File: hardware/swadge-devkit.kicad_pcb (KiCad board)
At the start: 2 copper layers, 63.7 x 100 mm, 61 parts, among them J1 USB_B_Micro, SW1 SW_SPDT, SW2 4-1437565-2, SW3 4-1437565-2, SW4 4-1437565-2, SW5 4-1437565-2, U1 ESP-13-WROOM-02D, U2 MCP6001-OT, U3 MSA300, U4 AP1117-33, U5 BUS_PCIexpress, U6 DISP_OLED_UG-2864HSWEG01, U7 SAO, U9 MMA8452Q

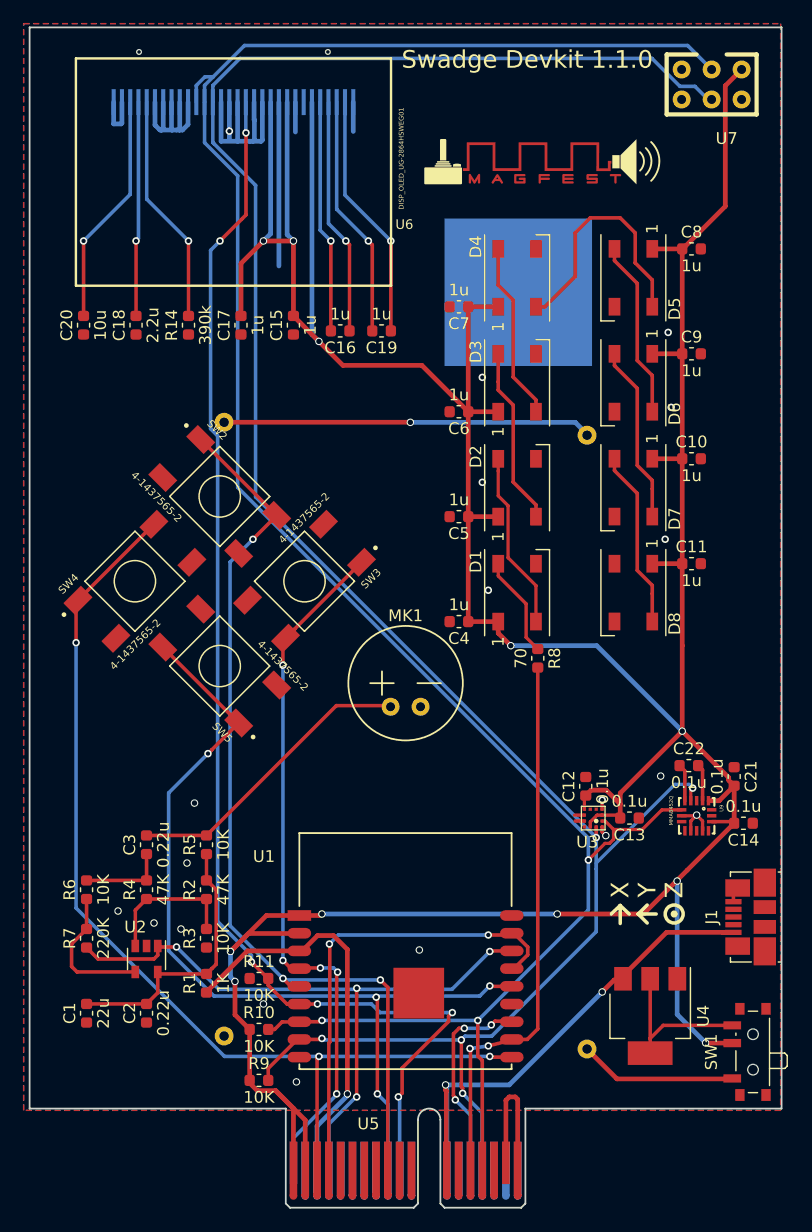
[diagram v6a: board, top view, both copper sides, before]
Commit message: #17 Reordered PCIe connector for WROOM sanity
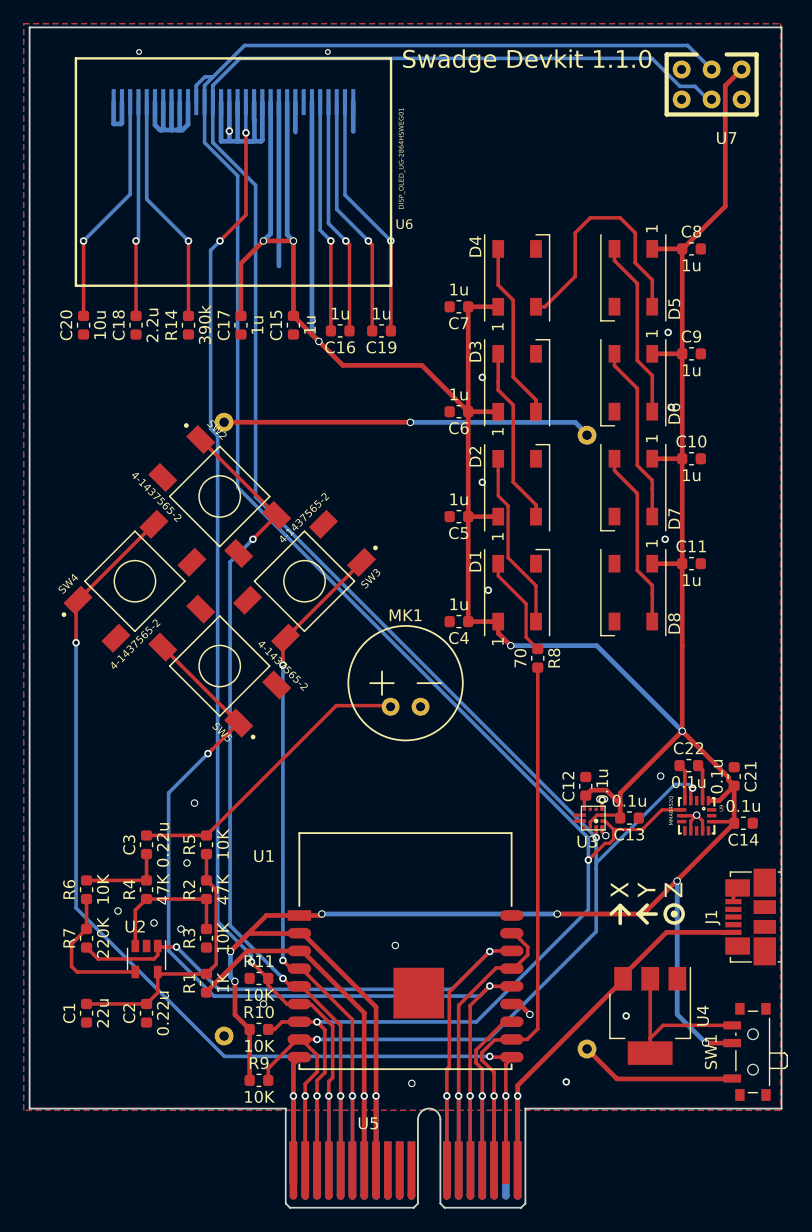
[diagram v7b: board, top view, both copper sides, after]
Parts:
- removed svg2mod: G***, Swadge_Parts:pcb_color_swatches
- removed svg2mod: G***, Swadge_Parts:MAGFEST_logo_centered_final
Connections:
- U5 pad A1: SW3 -> GND
- U5 pad A10: _RES -> Net-(U5-PadA10)
- U5 pad A12: +5V -> ADC_PIN
- U5 pad A13: Net-(U5-PadA13) -> REST
- U5 pad A14: TX -> SW5
- U5 pad A15: SCL -> TX
- U5 pad A16: Net-(U5-PadA16) -> RX
- U5 pad A17: Net-(U5-PadA17) -> SW4
- U5 pad A18: Net-(U5-PadA18) -> +5V
- U5 pad A2: Net-(U5-PadA2) -> SCL
- U5 pad A3: AUD_PWR -> SDA
- U5 pad A4: ADC_PIN -> _RES
- U5 pad A5: Net-(U5-PadA5) -> SW2
- U5 pad A6: Net-(U5-PadA6) -> SW3
- U5 pad A7: Net-(U5-PadA7) -> AUD_PWR
- U5 pad A8: Net-(U5-PadA8) -> +3V3
- U5 pad A9: SW5 -> Net-(U5-PadA9)
- U5 pad B1: +3V3 -> GND
- U5 pad B12: +5V -> ADC_PIN
- U5 pad B13: Net-(U5-PadB13) -> REST
- U5 pad B14: RX -> SW5
- U5 pad B15: SDA -> TX
- U5 pad B16: Net-(U5-PadB16) -> RX
- U5 pad B17: GND -> SW4
- U5 pad B18: GND -> +5V
- U5 pad B2: +3V3 -> SCL
- U5 pad B3: SW4 -> SDA
- U5 pad B4: REST -> _RES
- U5 pad B5: Net-(U5-PadB5) -> SW2
- U5 pad B6: Net-(U5-PadB6) -> SW3
- U5 pad B7: Net-(U5-PadB7) -> AUD_PWR
- U5 pad B8: Net-(U5-PadB8) -> +3V3
- U5 pad B9: SW2 -> Net-(U5-PadB9)
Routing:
- net +3V3: track 335.5 -> 346.8 mm, vias 11 -> 12
- net ADC_PIN: track 56.8 -> 66.6 mm, vias 4 -> 3
- net REST: track 39.2 -> 29.9 mm, vias 2 -> 1
- net SW5: track 76.8 -> 84.3 mm, vias 4 -> 3
- net +5V: track 45.1 -> 37.9 mm, vias 2 -> 1
- net SCL: track 188.7 -> 195.2 mm, vias 5 -> 4
- net _RES: track 109.7 -> 103.3 mm, vias 6 -> 4
- net SDA: track 187.0 -> 193.3 mm
- net SW4: track 86.9 -> 92.6 mm
- net RX: track 47.0 -> 52.6 mm, vias 2 -> 1
- net GND: track 82.0 -> 86.8 mm, vias 19 -> 23
- net SW3: track 59.7 -> 63.7 mm, vias 5 -> 3
- net TX: track 17.2 -> 20.6 mm, vias 3 -> 1
- net AUD_PWR: track 34.3 -> 37.1 mm
- net SW2: track 78.0 -> 76.9 mm
